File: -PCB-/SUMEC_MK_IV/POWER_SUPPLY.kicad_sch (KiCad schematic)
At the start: 1 part, among them J1 XT30PW-M

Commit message: I fucked up the repo?
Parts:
- added U?: TPS62133, Package_DFN_QFN:VQFN-16-1EP_3x3mm_P0.5mm_EP1.68x1.68mm_ThermalVias, symbol Regulator_Switching:TPS62133
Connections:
- new net: U?.1 (SW), U?.2 (SW), U?.3 (SW)
- new net: U?.10 (VIN), U?.11 (VIN), U?.12 (VIN)
- new net: U?.15 (GND), U?.16 (GND), U?.17 (GND), U?.6 (GND)
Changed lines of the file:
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@@
+	)
+	(symbol
+		(lib_id "Regulator_Switching:TPS62133")
+		(at 219.71 69.85 0)
+		(unit 1)
+		(exclude_from_sim no)
+		(in_bom yes)
+		(on_board yes)
+		(dnp no)
+		(fields_autoplaced yes)
+		(property "Reference" "U?"
+			(at 221.9341 54.61 0)
+			(effects
+				(font
+					(size 1.27 1.27)
+				)
+				(justify left)
+			)
+		)
+		(property "Value" "TPS62133"
+			(at 221.9341 57.15 0)
+			(effects
+				(font
+					(size 1.27 1.27)
+				)
+				(justify left)
+			)
+		)
+		(property "Footprint" "Package_DFN_QFN:VQFN-16-1EP_3x3mm_P0.5mm_EP1.68x1.68mm_ThermalVias"
+			(at 223.52 81.28 0)
+			(effects
+				(font
+					(size 1.27 1.27)
+				)
+				(justify left)
+				(hide yes)
+			)
+		)
+		(property "Datasheet" "http://www.ti.com/lit/ds/symlink/tps62130.pdf"
+			(at 219.71 69.85 0)
+			(effects
+				(font
+					(size 1.27 1.27)
+				)
+				(hide yes)
+			)
+		)
+		(property "Description" "3A Step-Down Converter with DCS-Control, Fixed 5.0V Output Voltage, 3-17V Input Voltage, QFN-16"
+			(at 219.71 69.85 0)
+			(effects
+				(font
+					(size 1.27 1.27)
+				)
+				(hide yes)
+			)
+		)
+		(pin "1"
+		)
+		(pin "10"
+		)
+		(pin "14"
+		)
+		(pin "3"
+		)
+		(pin "17"
+		)
+		(pin "9"
+		)
+		(pin "8"
+		)
+		(pin "5"
+		)
+		(pin "12"
+		)
+		(pin "7"
+		)
+		(pin "2"
+		)
+		(pin "11"
+		)
+		(pin "4"
+		)
+		(pin "6"
+		)
+		(pin "16"
+		)
+		(pin "15"
+		)
+		(pin "13"
+		)
+		(instances
+			(project ""
+				(path "/900bd7ac-cdf9-4a2f-8b1f-2c21e3760046/db21c0bc-8410-4aca-be63-6c1a31675c37"
+					(reference "U?")
+					(unit 1)
+				)
+			)
+		)
 	)
 	(symbol

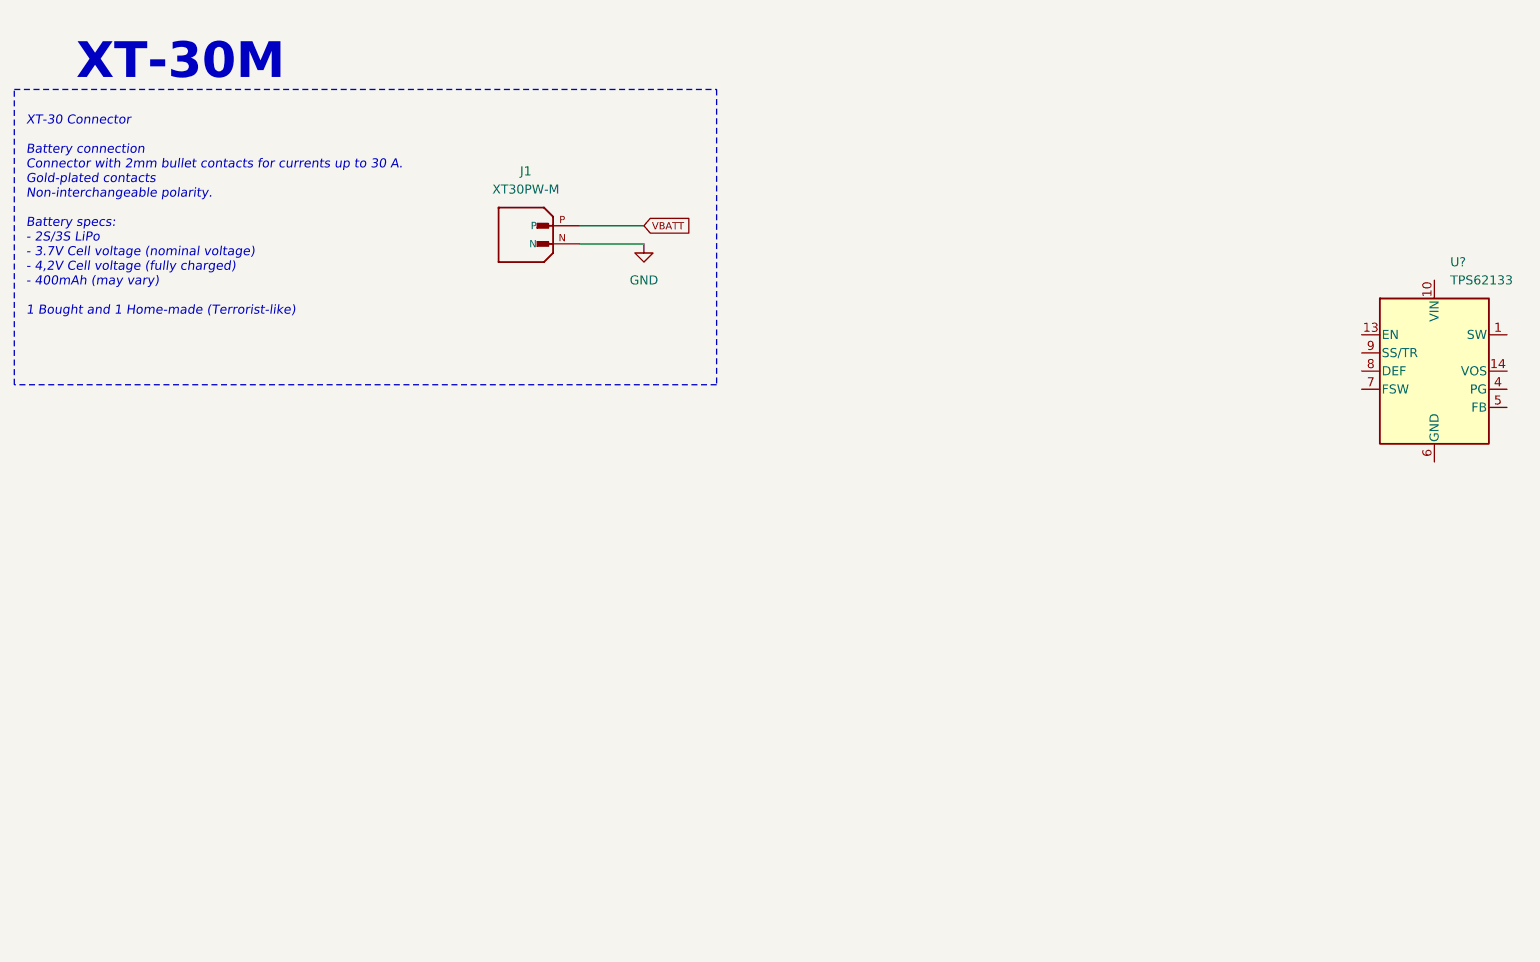
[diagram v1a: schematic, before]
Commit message: DC-DC conv added
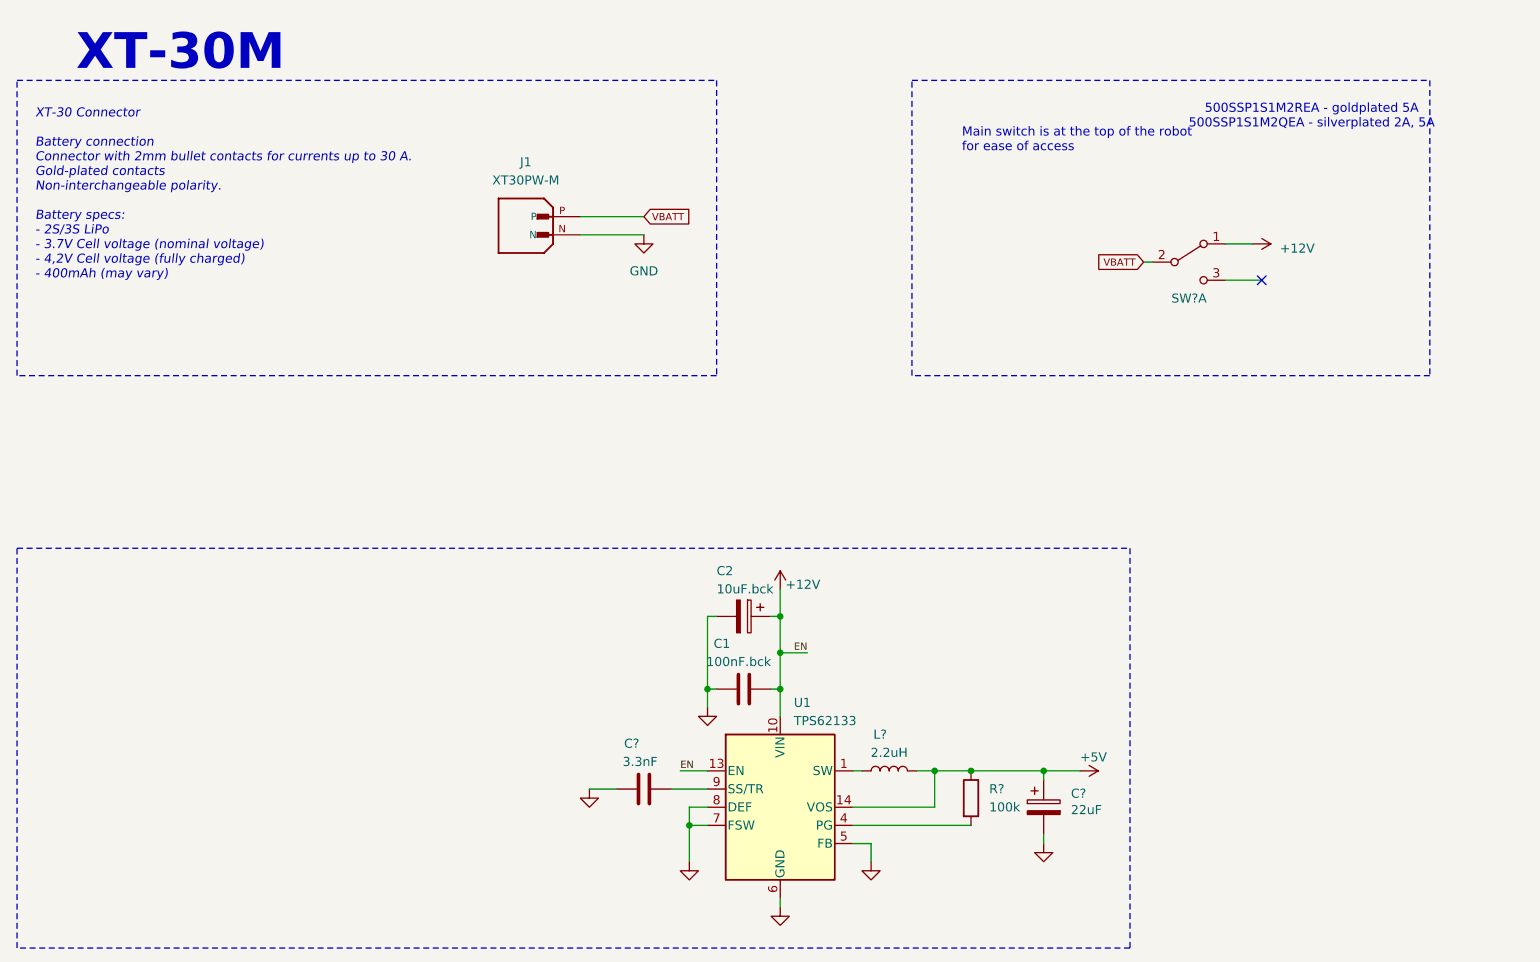
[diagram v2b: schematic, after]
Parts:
- added C1: 100nF.bck, Capacitor_SMD:C_0805_2012Metric_Pad1.18x1.45mm_HandSolder, symbol Device:C
- added C2: 10uF.bck, Capacitor_Tantalum_SMD:CP_EIA-3216-18_Kemet-A_Pad1.58x1.35mm_HandSolder, symbol Device:C_Polarized
- added C?: 3.3nF, Capacitor_SMD:C_0805_2012Metric_Pad1.18x1.45mm_HandSolder, symbol Device:C
- added C?: 22uF, symbol Device:C_Polarized
- added L?: 2.2uH, symbol Device:L
- added R?: 100k, symbol Device:R
- added SW?: SW_DPDT_x2, sumec-smdV2_library:Custom_SPDT_4.8mm_Switch, symbol Switch:SW_DPDT_x2
- gave numbers to parts that had none: 1
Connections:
- net GND: now also U1.15 (GND), U1.16 (GND), U1.17 (GND), U1.5 (FB), U1.6 (GND), U1.7 (FSW), U1.8 (DEF), C1.1, C2.2, C?.1, C?.2
- net VBATT: now also SW?.2 (B)
- net at U1.1 (SW), U1.2 (SW), U1.3 (SW): now also L?.1
- net +12V: now reaches U1.10 (VIN), U1.11 (VIN), U1.12 (VIN)
- net +12V: now also U1.13 (EN), C1.2, C2.1, SW?.1 (A)
- net +5V: now reaches U1.14 (VOS)
- net +5V: now also C?.1, L?.2, R?.1
- net at U1.4 (PG): now also R?.2
- net at U1.9 (SS/TR): now also C?.2
- no-connect marks 0 -> 1
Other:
- note added: "500SSP1S1M2REA - goldplated 5A 500SSP1S1M2QEA - silverplated 2A, 5A"
- note added: "Main switch is at the top of the robot for ease of access"
- note added: "XT-30 Connector Battery connection Connector with 2mm bullet contacts for currents up to 30 A. Gold-plated contacts Non-interchangeable polarity. Battery specs: - 2S/3S LiPo - 3.7V Cell voltage (nominal voltage) - 4,2V Cell voltage (fully charged) - 400mAh (may vary)"
- note removed: "XT-30 Connector Battery connection Connector with 2mm bullet contacts for currents up to 30 A. Gold-plated contacts Non-interchangeable polarity. Battery specs: - 2S/3S LiPo - 3.7V Cell voltage (nominal voltage) - 4,2V Cell voltage (fully charged) - 400mAh (may vary) 1 Bought and 1 Home-made (Terrorist-like)"
- company: (none) -> SPS NA PROSEKU
- title: (none) -> SUMEC_MK_IV
- moved on the sheet: J1, U1

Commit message: added stab. VBUS, USB connection
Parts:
- added C? (x2): 100nF, Capacitor_SMD:C_0805_2012Metric, symbol Device:C
- added C? (x2): 10uF.stabl, Capacitor_Tantalum_SMD:CP_EIA-3216-18_Kemet-A_Pad1.58x1.35mm_HandSolder, symbol Device:C_Polarized
- added C? (x4): 22uF, Capacitor_SMD:C_0805_2012Metric, symbol Device:C
- added D?: D_Schottky, symbol Device:D_Schottky
- added IC?: TPS565242DRLR, SOTFL50P160X60-6N, symbol SamacSys_Parts:TPS565242DRLR
- added L?: XAL4020-152MEB, XAL40XX, symbol SamacSys_Parts:XAL4020-222MEC
- added Q?: PMOS, symbol Simulation_SPICE:PMOS
- added R?: 10k, symbol Device:R
- added R?: 150k, Resistor_SMD:R_0805_2012Metric, symbol Device:R
- added R?: 100k, Resistor_SMD:R_0805_2012Metric, symbol Device:R
- added R?: 22k, Resistor_SMD:R_0805_2012Metric, symbol Device:R
- added R?: 33k, Resistor_SMD:R_0805_2012Metric, symbol Device:R
- added U?: LM1084-3.3, Package_TO_SOT_SMD:TO-263-3_TabPin2, symbol Regulator_Linear:LM1084-3.3
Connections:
- net +5V: now also C?.1, U?.3 (VI)
- net GND: now also C?.2, C?.2, C?.2, C?.2, C?.2, C?.2, C?.2, C?.2, IC?.3 (GND), IC?.4 (AGND), R?.2, R?.2, R?.2, U?.1 (GND)
- new net: Q?.2 (G), R?.1
- new net: IC?.6 (FB), R?.1, R?.2
- new net: IC?.2 (SW), L?.1
- new net +3V3: C?.1, U?.2 (VO)
- new net +BATT: C?.1, C?.1, IC?.1 (VIN), R?.1
- new net En_3V3: IC?.5 (EN), R?.1, R?.2
- new net VCC: C?.1, C?.1, C?.1, C?.1, L?.2, R?.1
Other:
- note added: "3v3"
- note added: "LOW Vf - DIODE LOW Rds - PMOS"
- moved on the sheet: C1, C2, C?, J1, L?, R?, SW?A, U1

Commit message: VBATT VBUS Switching
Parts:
- removed C1: 100nF.bck, Capacitor_SMD:C_0805_2012Metric_Pad1.18x1.45mm_HandSolder, symbol Device:C
- removed C2: 10uF.bck, Capacitor_Tantalum_SMD:CP_EIA-3216-18_Kemet-A_Pad1.58x1.35mm_HandSolder, symbol Device:C_Polarized
- added C1: 10uF.bck, Capacitor_Tantalum_SMD:CP_EIA-3216-18_Kemet-A_Pad1.58x1.35mm_HandSolder, symbol Device:C_Polarized
- added C2: 100nF.avin, Capacitor_SMD:C_0805_2012Metric_Pad1.18x1.45mm_HandSolder, symbol Device:C
- added D1: D_Schottky, symbol Device:D_Schottky
- gave numbers to parts that had none: 23
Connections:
- net +12V: now also C1.1, C2.1
- net +5V: now also D2.1 (K), D1.1 (K); no longer C14.1, L2.2, R5.1, U1.14 (VOS)
- net GND: now also C1.2, C2.2
- net VBUS 5V: now also D2.2 (A), Q1.2 (G), R6.1
- net at Q1.1 (D): now also D1.2 (A)
- net VOUT 5V: now reaches Q1.3 (S)
- net VOUT 5V: now also C14.1, L2.2, R5.1, U1.14 (VOS)
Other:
- moved on the sheet: C12, C14, D2, L2, Q1, R5, R6, SW1A

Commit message: power supp small change
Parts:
- removed C13: 10uF.stabl, Capacitor_Tantalum_SMD:CP_EIA-3216-18_Kemet-A_Pad1.58x1.35mm_HandSolder, symbol Device:C_Polarized
- added C?: 10uF.reg, Capacitor_Tantalum_SMD:CP_EIA-3216-18_Kemet-A_Pad1.58x1.35mm_HandSolder, symbol Device:C_Polarized
- C11: value 10uF.stabl -> 10uF.reg
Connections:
- net +3V3: now also C?.1
- net GND: now also C?.2
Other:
- note added: "LDO VOLTAGE REGULATOR"
- note added: "LM1084IS-3.3/NOPB LDO Voltage Regulator 3.3V/5A TO-263-3 Tab is output Max dropout voltage: 1.5V"
- moved on the sheet: C1, C10, C11, C12, C14, C2, C3, C4, C7, C8, C9, D1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

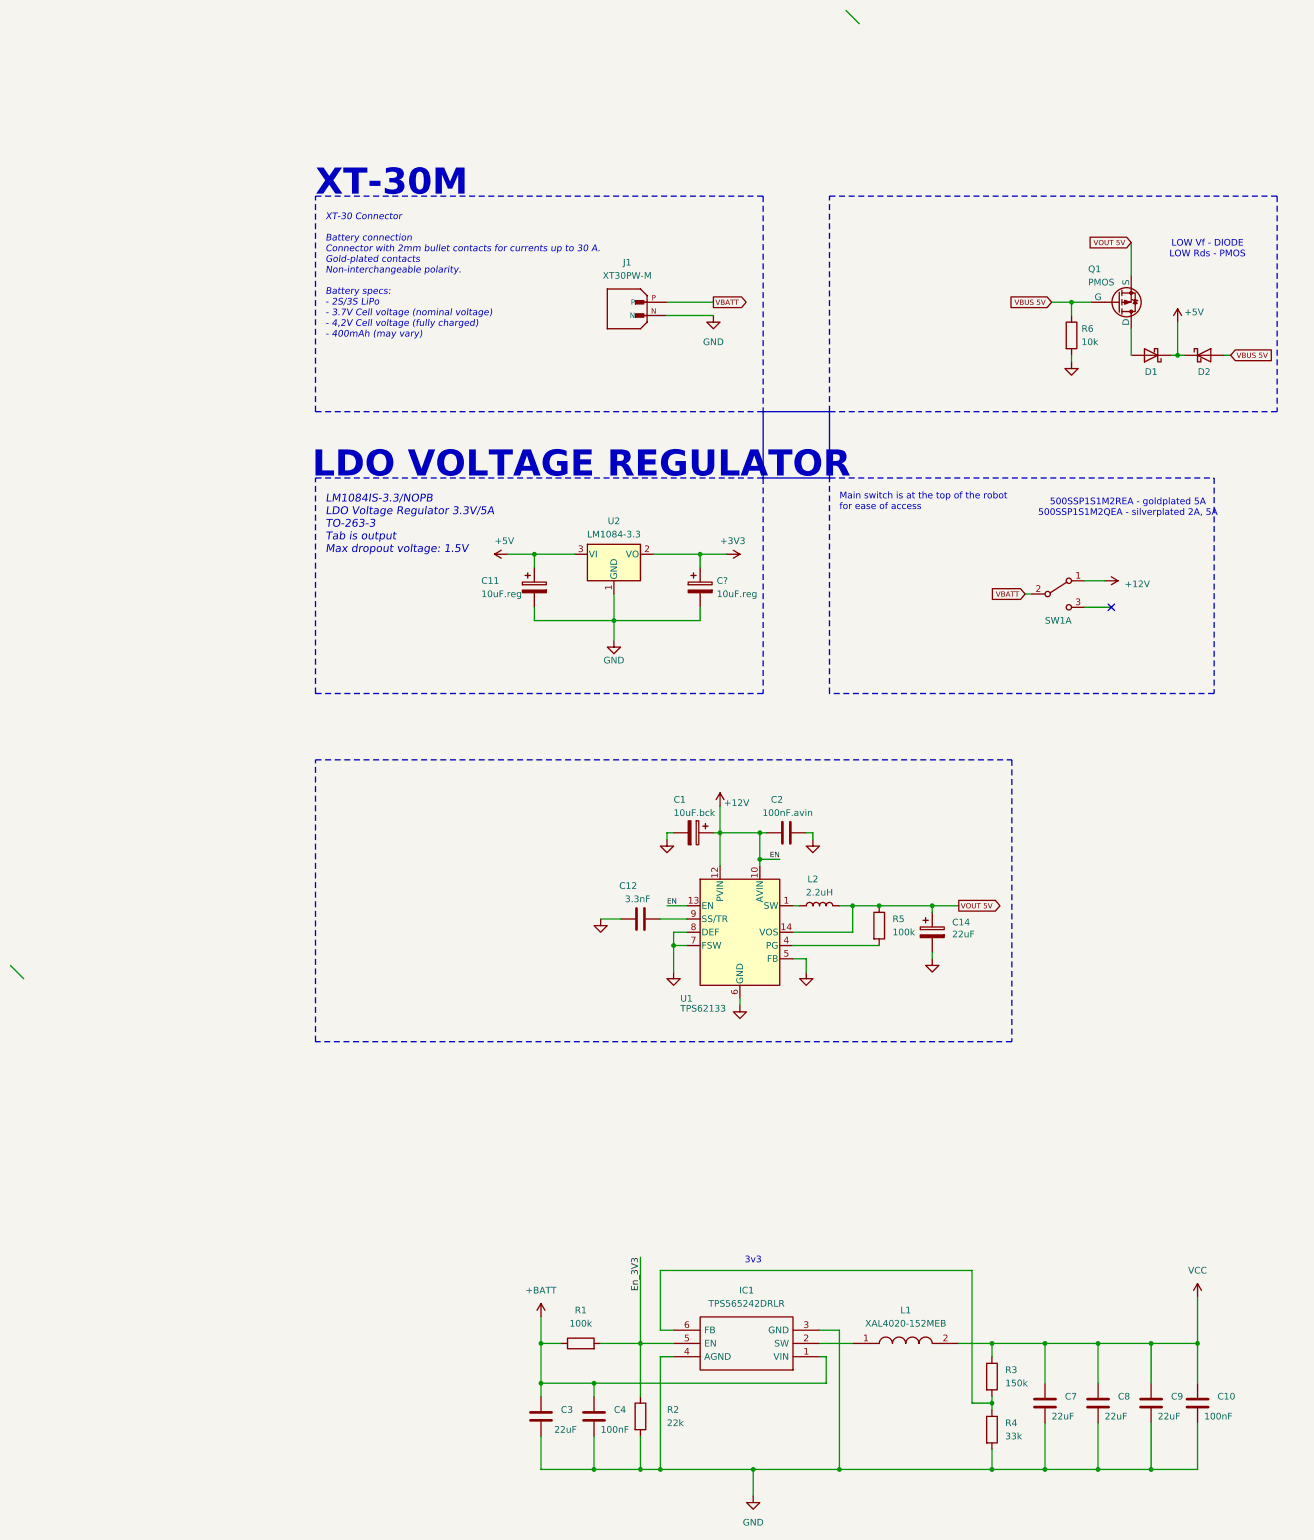
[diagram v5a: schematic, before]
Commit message: MK_IV update
Power supp sheet done, mechanical sheet almost done, some changes, updates etc.
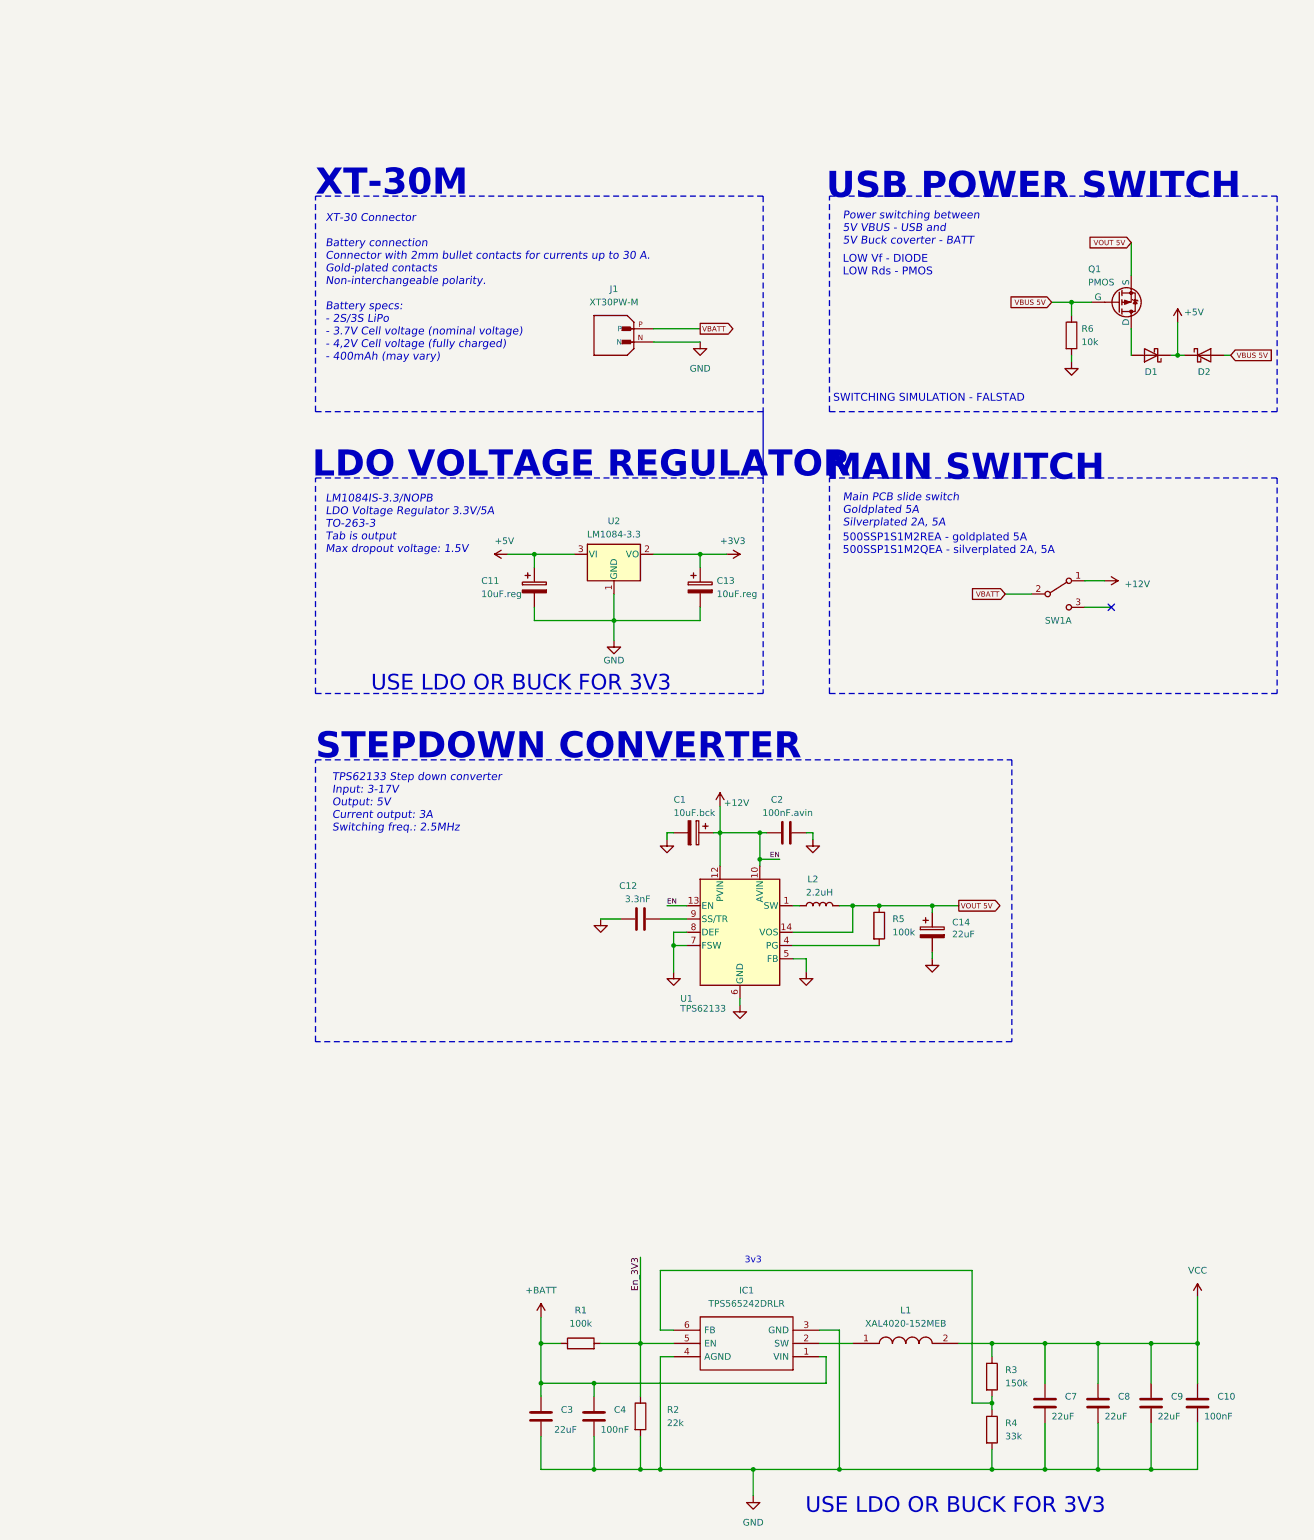
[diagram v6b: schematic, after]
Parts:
- gave numbers to parts that had none: 1
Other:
- note added: "MAIN SWITCH"
- note added: "Main PCB slide switch Goldplated 5A Silverplated 2A, 5A"
- note added: "Power switching between 5V VBUS - USB and 5V Buck coverter - BATT"
- note added: "STEPDOWN CONVERTER"
- note added: "SWITCHING SIMULATION - FALSTAD"
- note added: "TPS62133 Step down converter Input: 3-17V Output: 5V Current output: 3A Switching freq.: 2.5MHz"
- note added: "USB POWER SWITCH"
- note added: "USE LDO OR BUCK FOR 3V3"
- note removed: "Main switch is at the top of the robot for ease of access"
- moved on the sheet: J1
